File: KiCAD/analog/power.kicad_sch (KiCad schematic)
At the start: 27 parts, among them J33 Screw_Terminal_01x02, J34 Screw_Terminal_01x02, J5 Screw_Terminal_01x02, K5 G6RL-1-DC12, U13 MCP1700x-330xxTO, U6 LM2940CT-5.0, U7 LT1054, U8 LM2940CT-12

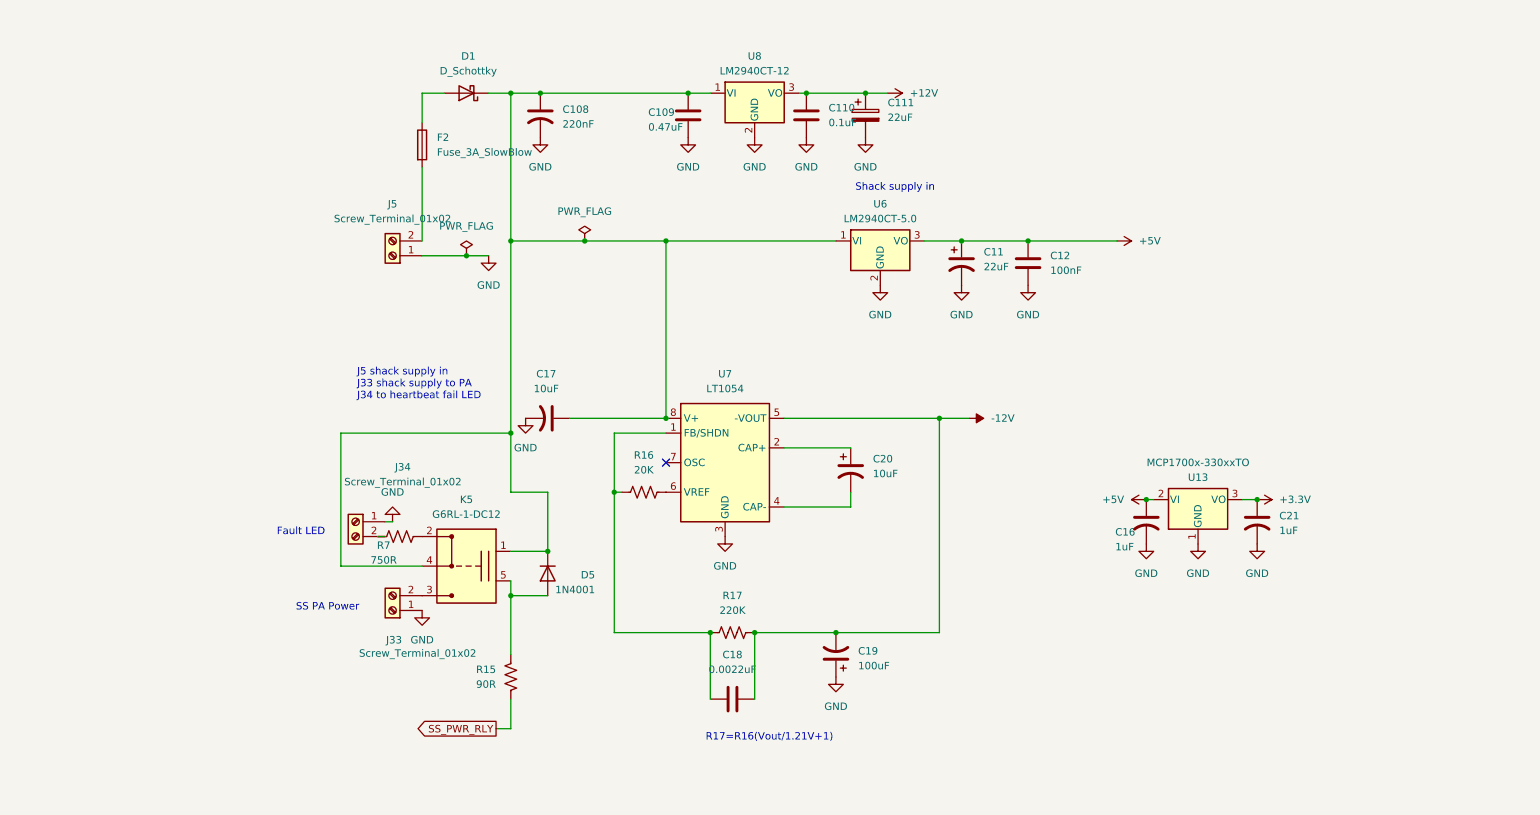
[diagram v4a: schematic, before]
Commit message: revD analog: L1 Bourns 78F footprint + CD74HC4050E xmitter lib additions
Analog L1 (270nH Bourns 78F RF choke) gets footprint
Inductor_THT:L_Axial_L7.0mm_D3.3mm_P10.16mm_Horizontal_Fastron_MICC
(stock KiCad; 78F body 7.11x2.79mm fits within the MICC silk envelope).

Added to xmitter library:
- symbol CD74HC4050E (hex non-inverting buffer, DIP-16, standard 4050
  pinout, pre-linked to xmitter:DIP-16_W7.62mm footprint)
- footprint xmitter:DIP-16_W7.62mm (verbatim copy of stock
  Package_DIP:DIP-16_W7.62mm so the lib is self-contained)

Other sheet / project / netlist touches picked up from the recent
session work on analog test sheet and protoshield.

Co-Authored-By: Claude Opus 4.7 <noreply@anthropic.com>
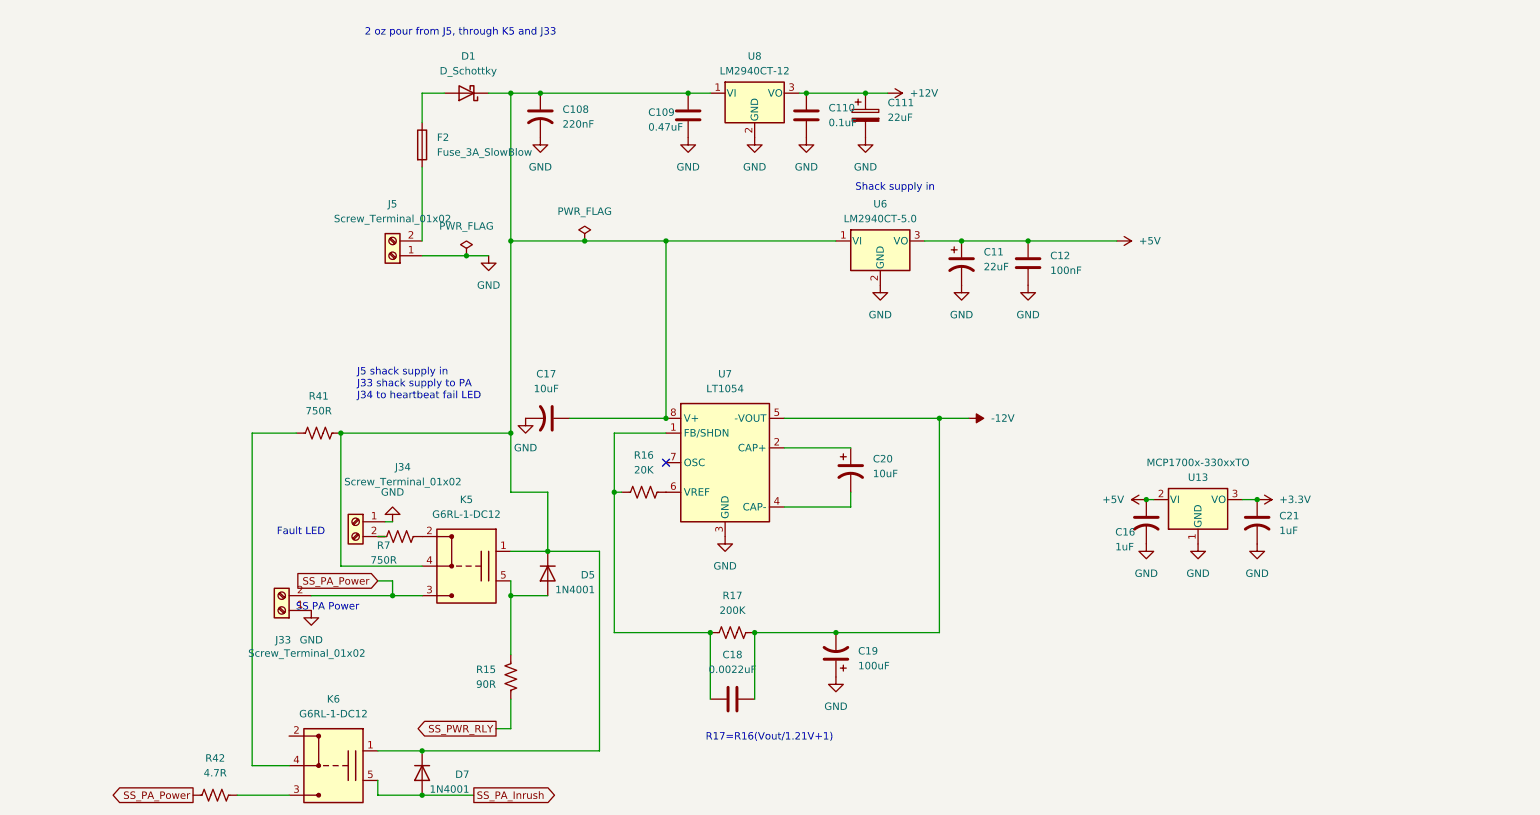
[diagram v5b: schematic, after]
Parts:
- added D7: 1N4001, Diode_THT:D_DO-41_SOD81_P10.16mm_Horizontal, symbol Diode:1N4001
- added K6: G6RL-1-DC12, xmitter:Relay_SPDT_Omron_G6RL-1, symbol xmitter:Relay_SPDT_G6RL
- added R41: 750R, symbol Device:R_US
- added R42: 4.7R, symbol Device:R_US
- D1: footprint (none) -> Diode_THT:D_DO-201AD_P15.24mm_Horizontal
- R17: value 220K -> 200K
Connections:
- net at C108.1, C109.1, C17.1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: now also D7.1 (K), K6.1 (coil+), R41.2
- net SS_PA_Power: now reaches J33.2 (Pin_2), K5.3 (NO)
- net SS_PA_Power: now also R42.1
- new net: K6.4 (COM), R41.1
- new net: K6.3 (NO), R42.2
- new net SS_PA_Inrush: D7.2 (A), K6.5 (coil-)
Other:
- note added: "2 oz pour from J5, through K5 and J33"
- moved on the sheet: J33

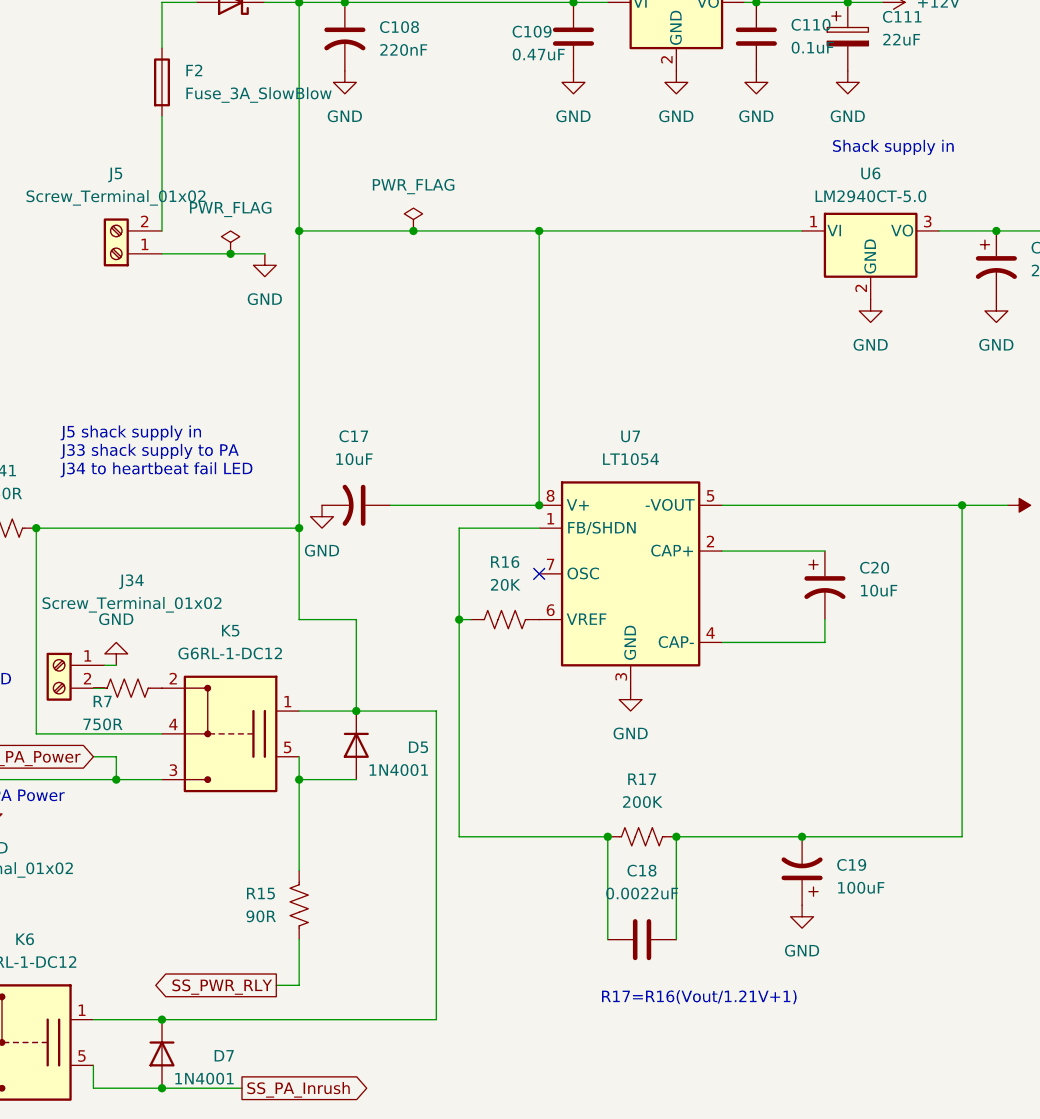
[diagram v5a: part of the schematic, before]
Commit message: revD analog power: modify +5V regulator path
Add R43 (15R), R44 (90R), C29, C31 to the +5V regulator path on
power.kicad_sch, plus two local GND symbols. Pre-dropper + decoupling
refinement to reduce LM2940CT-5.0 input voltage headroom and ease
thermal dissipation.

Co-Authored-By: Claude Opus 4.7 <noreply@anthropic.com>
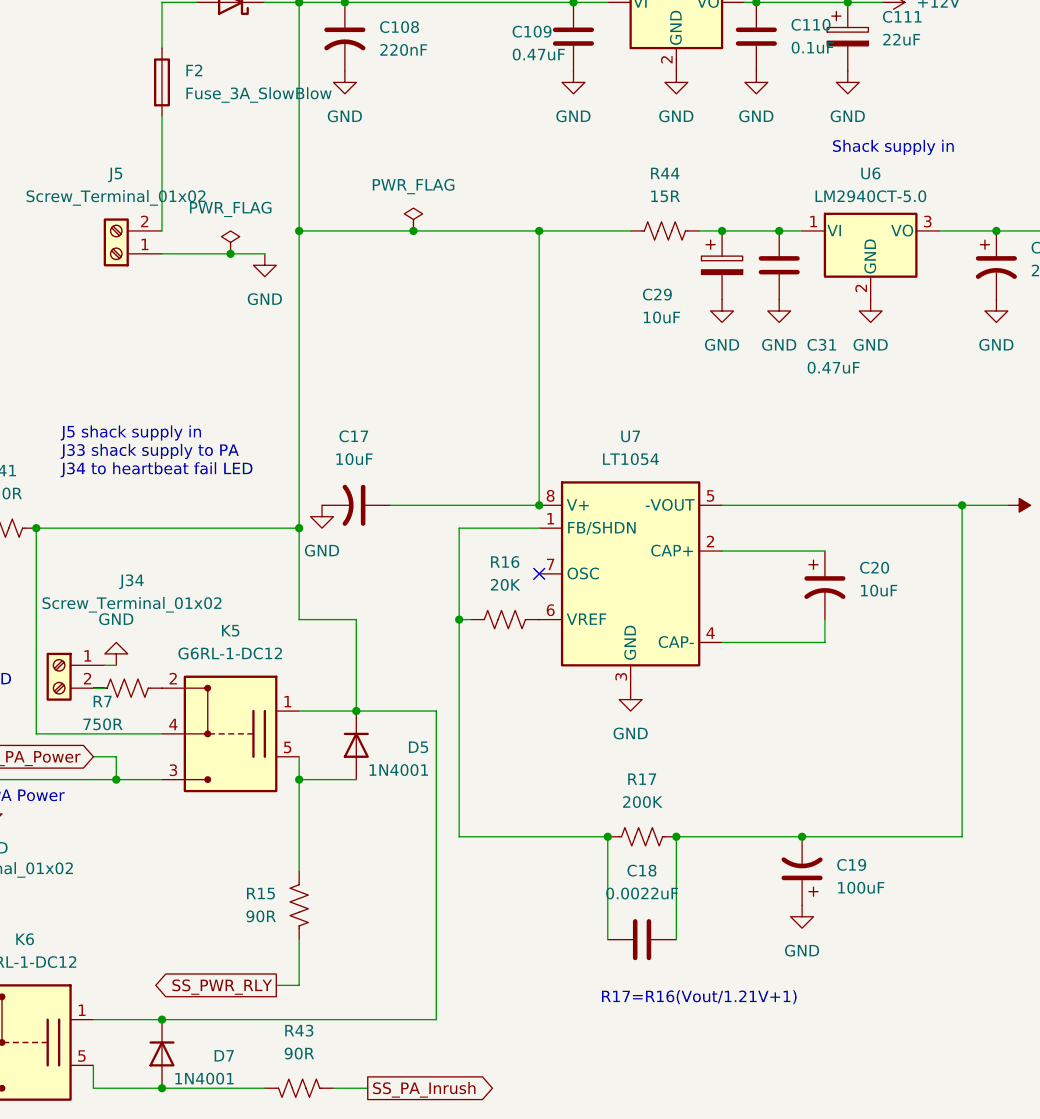
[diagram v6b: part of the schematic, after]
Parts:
- added C29: 10uF, symbol Device:C_Polarized
- added C31: 0.47uF, symbol Device:C
- added R43: 90R, Resistor_THT:R_Axial_DIN0207_L6.3mm_D2.5mm_P10.16mm_Horizontal, symbol Device:R_US
- added R44: 15R, symbol Device:R_US
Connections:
- net GND: now also C29.2, C31.2
- net SS_PA_Inrush: now also R43.2; no longer D7.2 (A), K6.5 (coil-)
- net at C108.1, C109.1, C17.1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: now also R44.1; no longer U6.1 (VI)
- new net: C29.1, C31.1, R44.2, U6.1 (VI)
- new net: D7.2 (A), K6.5 (coil-), R43.1

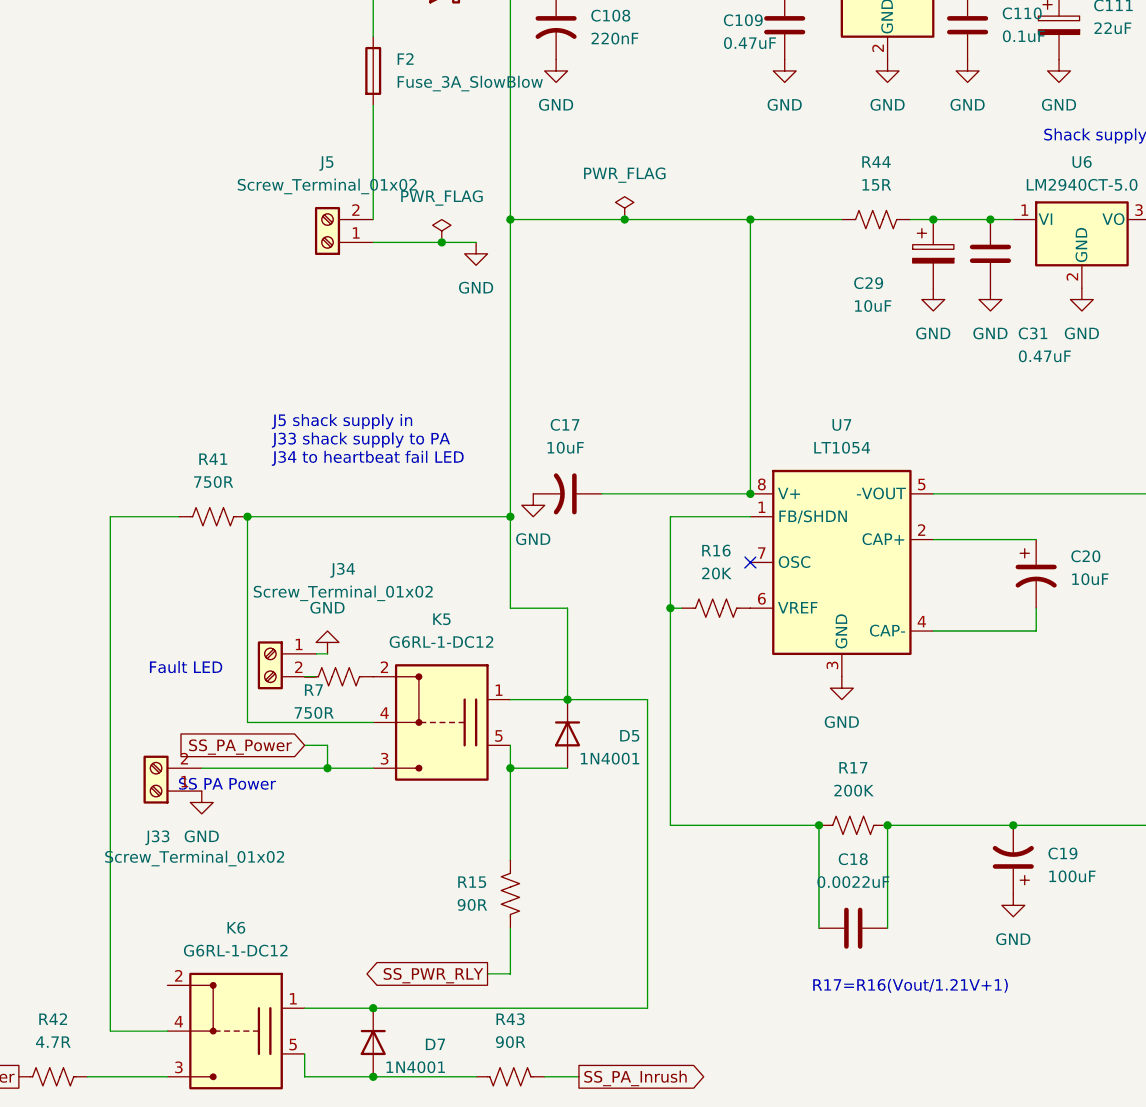
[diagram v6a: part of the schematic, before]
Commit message: revD: ss_pa U13 LM2936 pinout fix + analog U9 74HCT125 miswiring fix
ss_pa fault_shutdown.kicad_sch: fix U13 pin-to-signal mapping so an
LM2936Z-5.0/NOPB can be installed without destruction (prior MCP1700
symbol had pin 1=GND, 2=VI, 3=VO; LM2936 datasheet is pin 1=VO, 2=GND,
3=VI).

analog dac.kicad_sch: fix U9 74HCT125 miswiring found during follow-up
audit.

Co-Authored-By: Claude Opus 4.7 <noreply@anthropic.com>
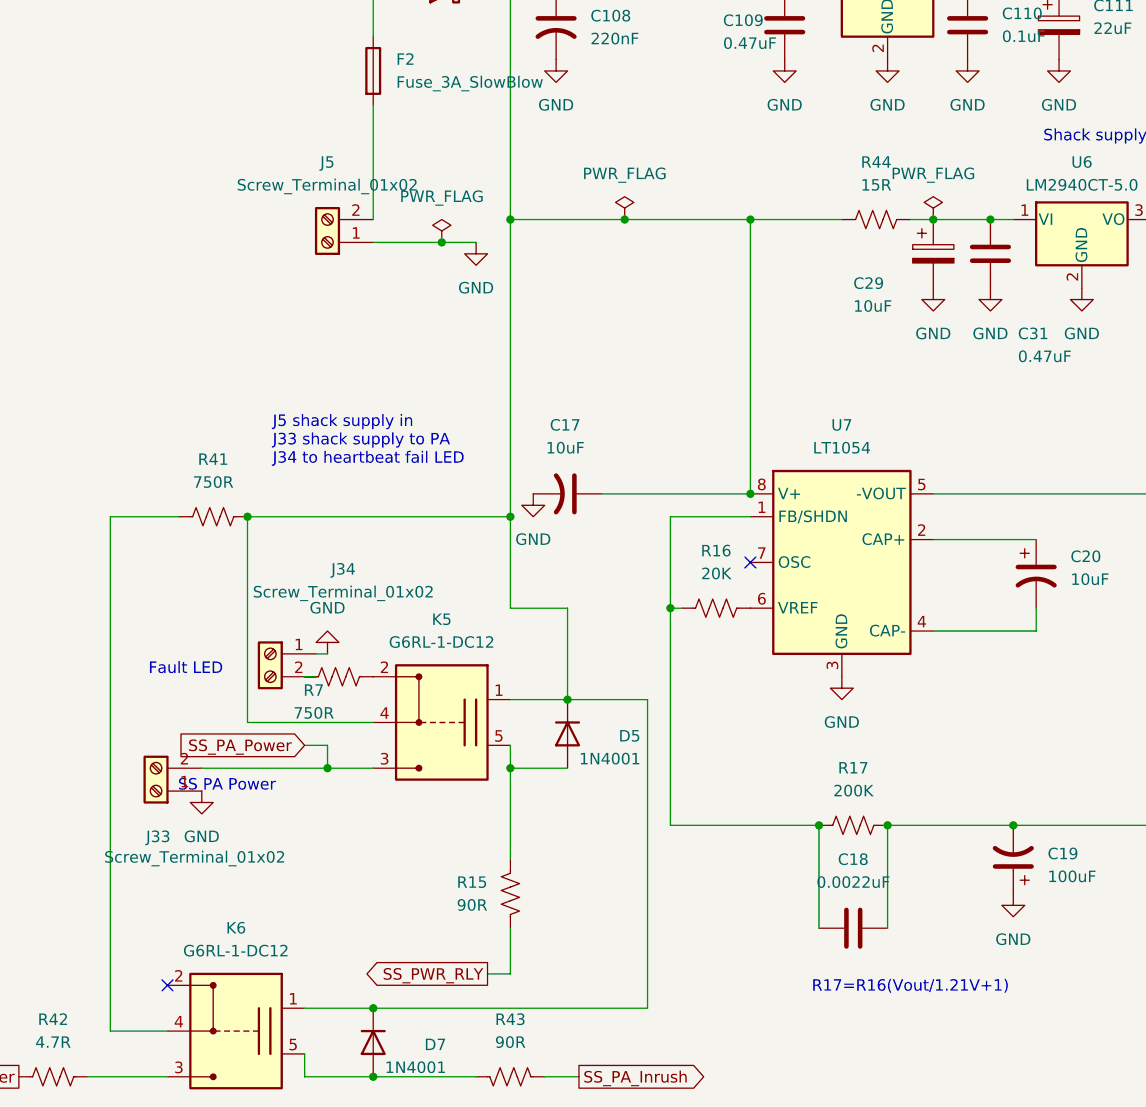
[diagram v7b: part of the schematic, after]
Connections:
- no-connect marks 1 -> 2
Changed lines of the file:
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@@
 	)
 	(no_connect
+		(at 59.69 152.4)
+	)
+	(no_connect
 		(at 124.46 105.41)
 	)
@@
 					(unit 1)
 				)
+			)
+		)
+	)
+	(symbol
+		(lib_id "power:PWR_FLAG")
+		(at 144.78 67.31 0)
+		(unit 1)
+		(body_style 1)
+		(exclude_from_sim no)
+		(in_bom yes)
+		(on_board yes)
+		(in_pos_files yes)
+		(dnp no)
+		(fields_autoplaced yes)
+		(property "Reference" "#FLG04"
+			(at 144.78 65.405 0)
+			(hide yes)
+			(show_name no)
+			(do_not_autoplace no)
+			(effects
+				(font
+					(size 1.27 1.27)
+				)
+			)
+		)
+		(property "Value" "PWR_FLAG"
+			(at 144.78 62.23 0)
+			(show_name no)
+			(do_not_autoplace no)
+			(effects
+				(font
+					(size 1.27 1.27)
+				)
+			)
+		)
+		(property "Footprint" ""
+			(at 144.78 67.31 0)
+			(hide yes)
+			(show_name no)
+			(do_not_autoplace no)
+			(effects
+				(font
+					(size 1.27 1.27)
+				)
+			)
+		)
+		(property "Datasheet" ""
+			(at 144.78 67.31 0)
+			(hide yes)
+			(show_name no)
+			(do_not_autoplace no)
+			(effects
+				(font
+					(size 1.27 1.27)
+				)
+			)
+		)
+		(property "Description" "Special symbol for telling ERC where power comes from"
+			(at 144.78 67.31 0)
+			(hide yes)
+			(show_name no)
+			(do_not_autoplace no)
+			(effects
+				(font
+					(size 1.27 1.27)
+				)
+			)
+		)
+		(pin "1"
+		)
+		(instances
+			(project "analog"
+				(path "/d3de40b8-856b-4fbd-829c-f45ffcd55742/9d33972e-4f39-4043-b71d-952850d73035"
+					(reference "#FLG04")
+					(unit 1)
+				)
